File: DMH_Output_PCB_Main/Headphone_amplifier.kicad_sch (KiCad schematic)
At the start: 20 parts, among them J12 Conn_01x06_PinHeader, J27 Conn_01x06_PinHeader, U11 TL074, U13 NE5532, U15 NE5532

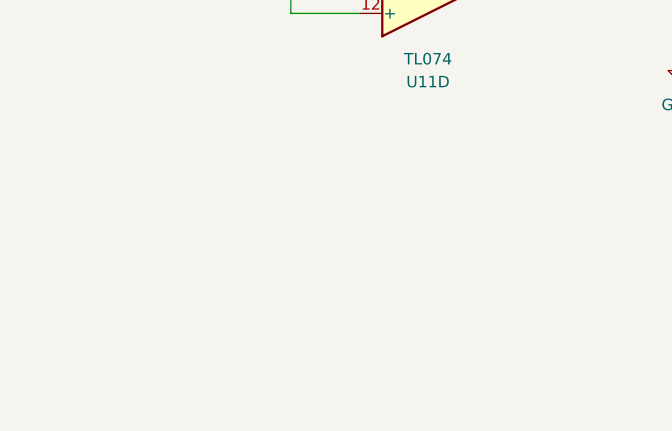
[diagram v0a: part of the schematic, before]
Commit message: Placed pin sockets
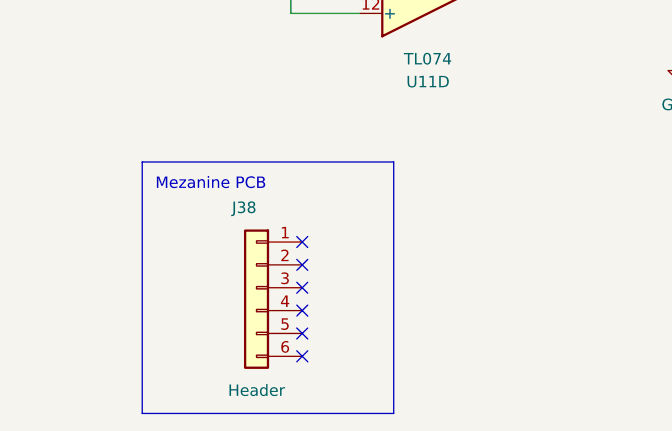
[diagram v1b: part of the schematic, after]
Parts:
- added J38: Conn_01x06, Connector_PinHeader_2.54mm:PinHeader_1x06_P2.54mm_Vertical, symbol Connector_Generic:Conn_01x06
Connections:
- no-connect marks 0 -> 6
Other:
- note added: "Mezanine PCB"
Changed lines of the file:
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@@
+		)
+	)
+	(rectangle
+		(start 25.4 162.56)
+		(end 53.34 190.5)
+		(stroke
+			(width 0)
+			(type default)
+		)
+		(fill
+			(type none)
 		)
 	)
@@
 		)
 	)
+	(text "Mezanine PCB"
+		(exclude_from_sim no)
+		(at 33.02 165.1 0)
+		(effects
+			(font
+				(size 1.27 1.27)
+			)
+		)
+	)
 	(junction
 		(at 105.41 120.65)
@@
 		(diameter 0)
 		(color 0 0 0 0)
+	)
+	(no_connect
+		(at 43.18 176.53)
+	)
+	(no_connect
+		(at 43.18 181.61)
+	)
+	(no_connect
+		(at 43.18 179.07)
+	)
+	(no_connect
+		(at 43.18 171.45)
+	)
+	(no_connect
+		(at 43.18 173.99)
+	)
+	(no_connect
+		(at 43.18 184.15)
 	)
 	(wire
@@
 				)
 			)
+		)
+	)
+	(symbol
+		(lib_id "Connector_Generic:Conn_01x06")
+		(at 38.1 176.53 0)
+		(mirror y)
+		(unit 1)
+		(body_style 1)
+		(exclude_from_sim no)
+		(in_bom yes)
+		(on_board no)
+		(in_pos_files yes)
+		(dnp no)
+		(property "Reference" "J38"
+			(at 38.1 167.64 0)
+			(show_name no)
+			(do_not_autoplace no)
+			(effects
+				(font
+					(size 1.27 1.27)
+				)
+				(justify left)
+			)
+		)
+		(property "Value" "Conn_01x06"
+			(at 38.1 186.69 0)
+			(hide yes)
+			(show_name no)
+			(do_not_autoplace no)
+			(effects
+				(font
+					(size 1.27 1.27)
+				)
+			)
+		)
+		(property "Footprint" "Connector_PinHeader_2.54mm:PinHeader_1x06_P2.54mm_Vertical"
+			(at 38.1 176.53 0)
+			(hide yes)
+			(show_name no)
+			(do_not_autoplace no)
+			(effects
+				(font
+					(size 1.27 1.27)
+				)
+			)
+		)
+		(property "Datasheet" ""
+			(at 38.1 176.53 0)
+			(hide yes)
+			(show_name no)
+			(do_not_autoplace no)
+			(effects
+				(font
+					(size 1.27 1.27)
+				)
+			)
+		)
+		(property "Description" "Header"
+			(at 38.1 187.96 0)
+			(show_name no)
+			(do_not_autoplace no)
+			(effects
+				(font
+					(size 1.27 1.27)
+				)
+			)
+		)
+		(property "Function" ""
+			(at 38.1 176.53 0)
+			(show_name no)
+			(do_not_autoplace no)
+			(effects
+				(font
+					(size 1.27 1.27)
+				)
+			)
+		)
+		(pin "2"
+		)
+		(pin "6"
+		)
+		(pin "1"
+		)
+		(pin "5"
+		)
+		(pin "3"
+		)
+		(pin "4"
+		)
+		(instances
+			(project "DMH_Output_PCB_Main"
+				(path "/58f4306d-5387-4983-bb08-41a2313fd315/45b3c00a-420e-4349-b096-199706c640d6"
+					(reference "J38")
+					(unit 1)
+				)
+			)
